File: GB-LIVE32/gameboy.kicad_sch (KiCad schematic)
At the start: 16 parts

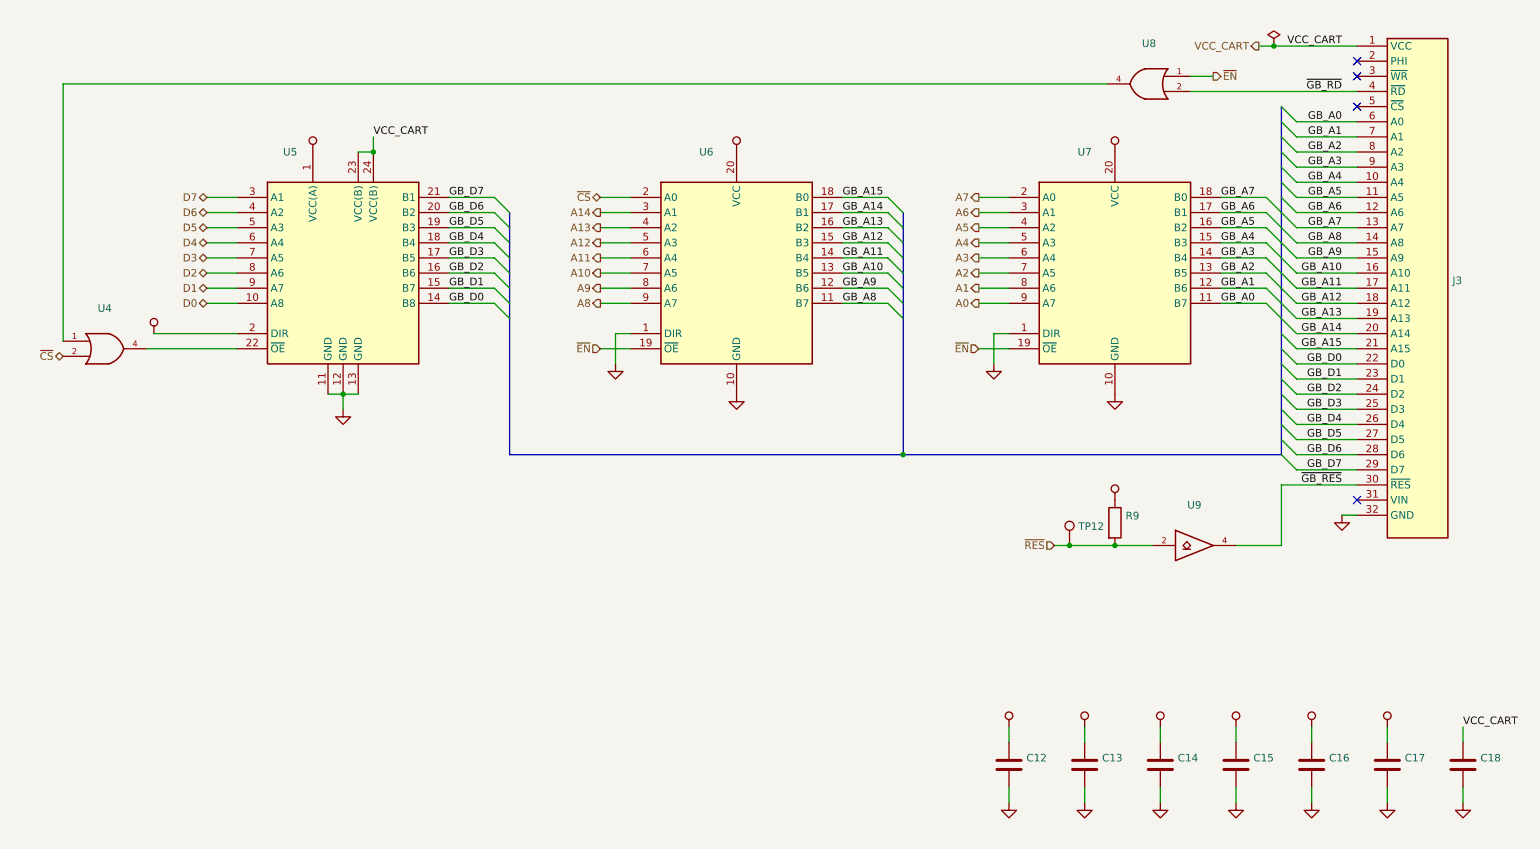
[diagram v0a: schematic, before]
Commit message: Upgrade projects to KiCad 7
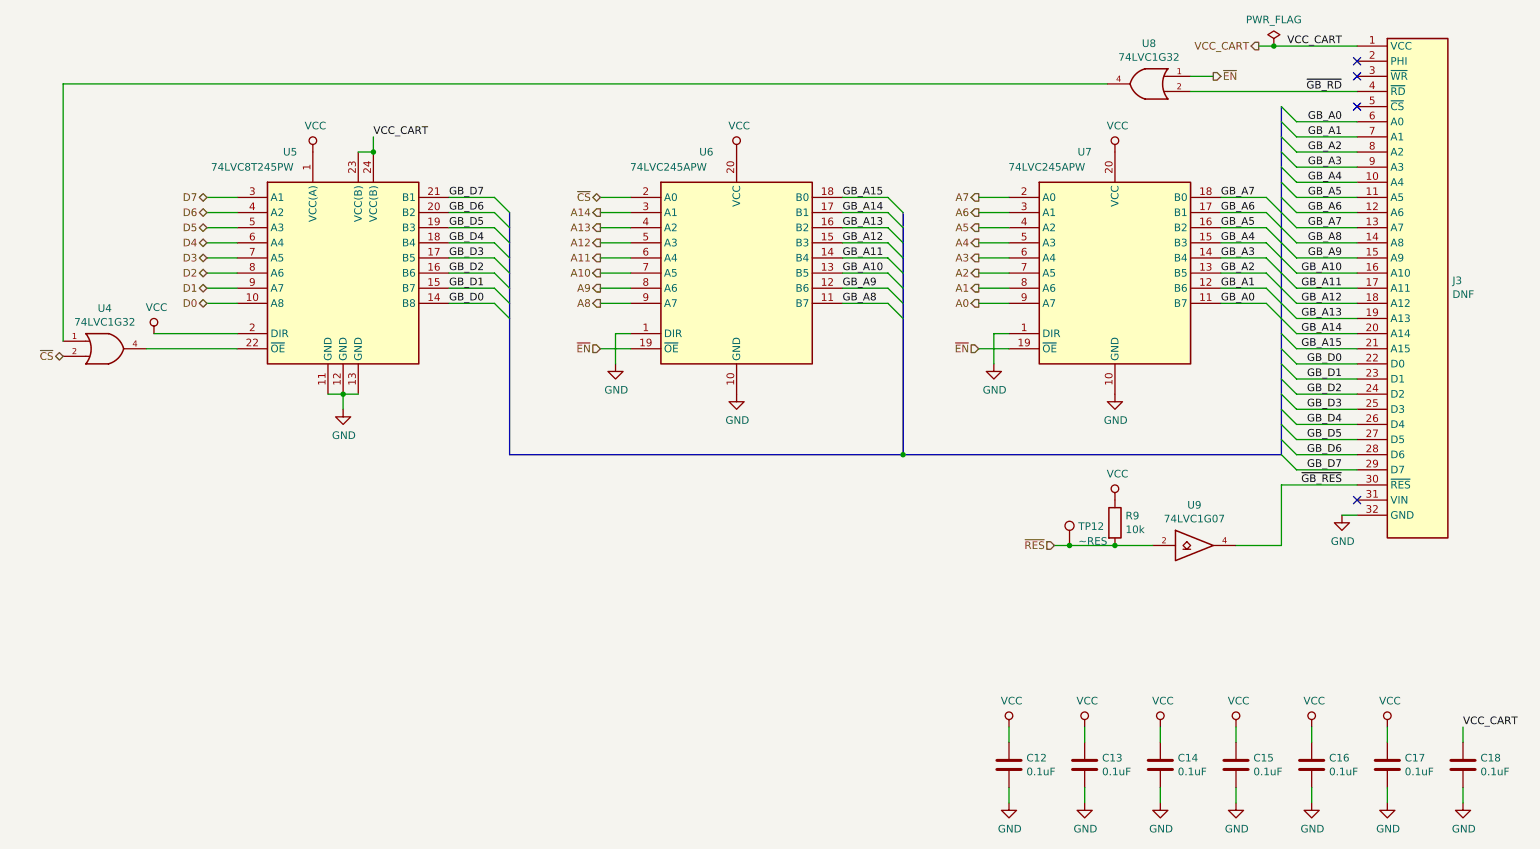
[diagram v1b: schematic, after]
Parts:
- C12, C13, C14, C15, C16, C17, C18: value (none) -> 0.1uF; footprint (none) -> Capacitor_SMD:C_0603_1608Metric
- J3: value (none) -> DNF; footprint (none) -> Gekkio_Connector_PCBEdge:GameBoy_Cartridge_1x32_P1.50mm_Edge
- R9: value (none) -> 10k; footprint (none) -> Resistor_SMD:R_0603_1608Metric
- TP12: value (none) -> ~RES; footprint (none) -> TestPoint:TestPoint_Pad_D1.0mm
- U4, U8: value (none) -> 74LVC1G32; footprint (none) -> Package_TO_SOT_SMD:SOT-353_SC-70-5
- U5: value (none) -> 74LVC8T245PW; footprint (none) -> Package_SO:TSSOP-24_4.4x7.8mm_P0.65mm
- U6, U7: value (none) -> 74LVC245APW; footprint (none) -> Package_SO:TSSOP-20_4.4x6.5mm_P0.65mm
- U9: value (none) -> 74LVC1G07; footprint (none) -> Package_TO_SOT_SMD:SOT-353_SC-70-5
